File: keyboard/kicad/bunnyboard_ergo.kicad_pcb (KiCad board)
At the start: 2 copper layers, 253.5 x 103.8 mm, 58 parts, among them U2 Pico

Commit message: ergo: Pitch V2 dokumentiert, Logo mitverschoben, neu geroutet
- README: Abschnitt 'ergo variant' mit Pitch-Entscheidung (V1 Kuppenmass
  verwworfen: 0.5 mm Cap-Luecke Ring/Mittel; V2 19-mm-Raster: 4.0 mm),
  GAP-120-Begruendung und Outline-Herkunft
- vergleich_pitch.py auf GAP 120 nachgezogen (war 96)
- Kupfer-Logo G*** mitverschoben: lag nach dem Transform ausserhalb von
  Edge.Cuts (Quelle 140.69/119.17 -> Ziel frei ueber der Bank, 104/-30)
- Pipeline neu gelaufen: 260 Tracks+Vias, 0 DRC, 0 unconnected,
  0 Footprints ausserhalb des Umrisses
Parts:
- moved G*** 153.6 mm to (104.0, -30.0)

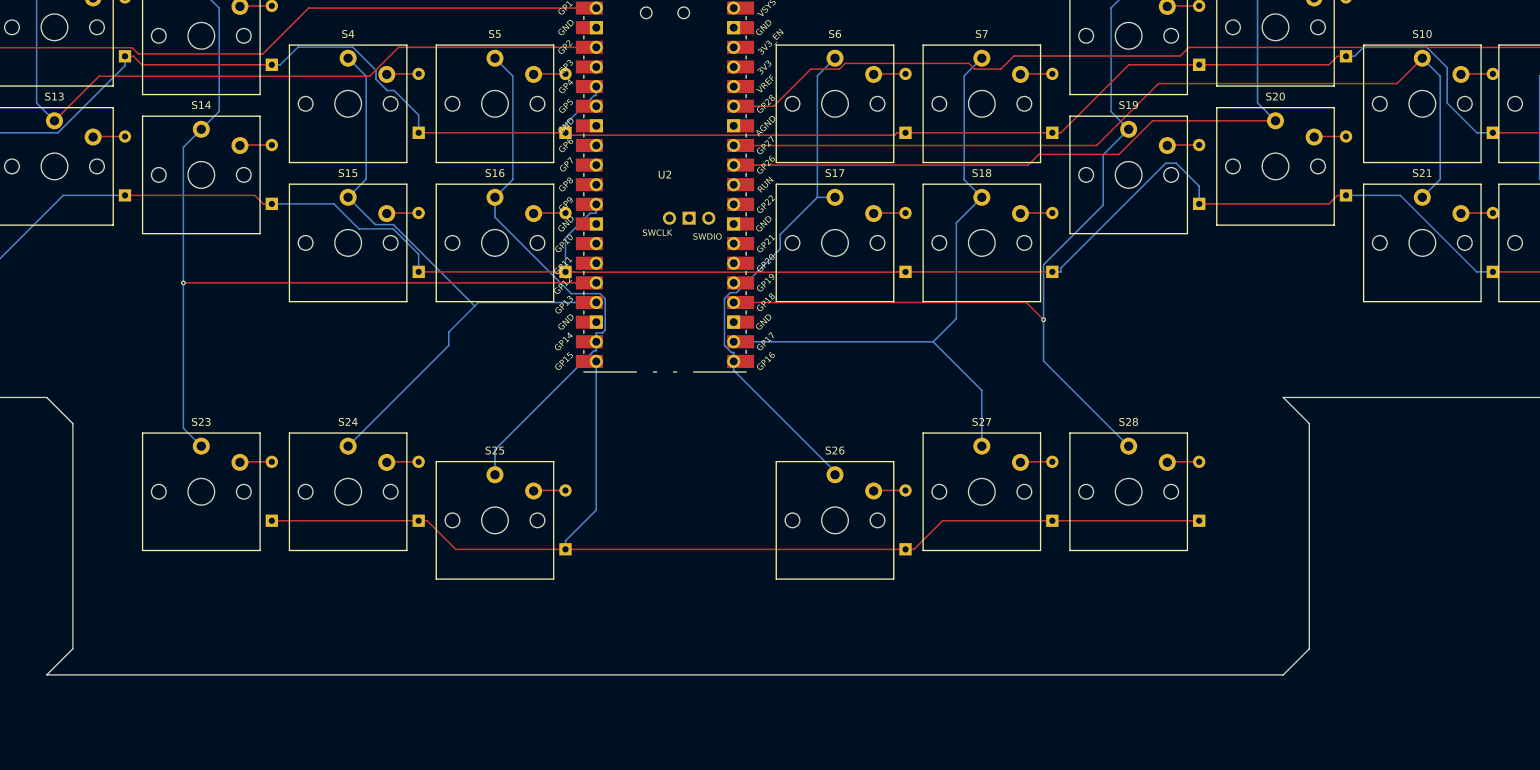
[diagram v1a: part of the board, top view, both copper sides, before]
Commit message: ergo: Daumen-Cluster korrigiert (S23/S25 vertauscht), Produktionsdaten, Viewer
Fehler gefunden beim Vergleich Quell- vs Zielboard:
- Daumen-y war S23/S28=41.0 und S25/S26=44.7 - vertauscht. STAGGER.md:
  Taste1 (A/E, Ruhepunkt) +45, Taste2 (O/U, 19 innen) +41, Extra X1/X2 +55.
  Jetzt S23/S28=44.7, S24/S27=41.0, S25/S26=55.0.
- keyboard/production/gerber.zip war das ORIGINAL vom 11.03.2024, nicht das
  Ergo-Board. Neu: keyboard/production/gerber_ergo.zip (26 Dateien) mit
  frischen Gerbern, Drill und positions.csv.

docs/ergebnis.html: selbsttragender Viewer (Bilder inline + massstaeblicher
SVG-Routingplan + Verifikationstabelle).

Verifikation: 252 Tracks, 0 DRC, 0 unconnected, min Daumen-Kappenabstand
4.36 mm, Viewer in Chromium fehlerfrei (3 Bilder dekodiert, 249 Track-Linien).
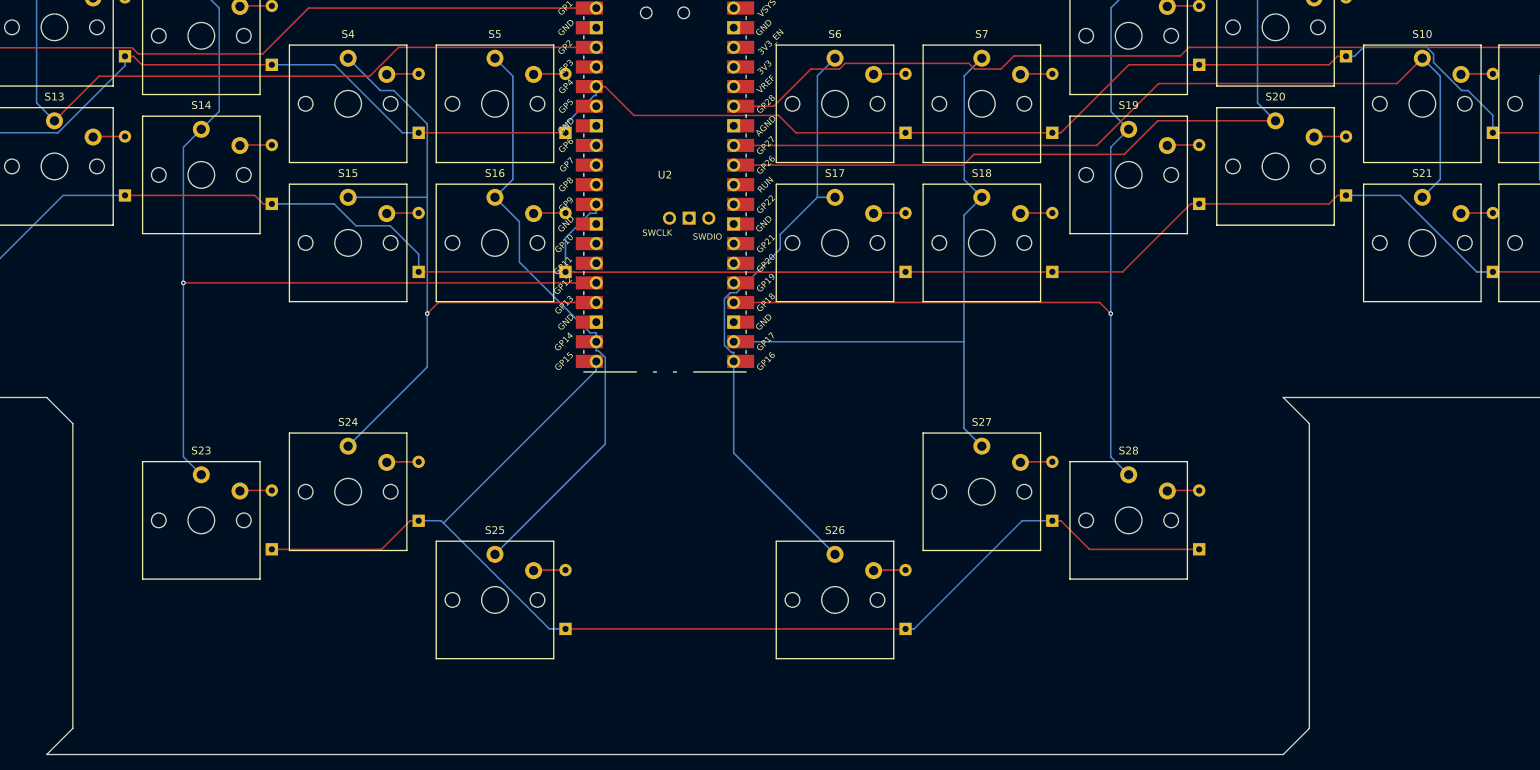
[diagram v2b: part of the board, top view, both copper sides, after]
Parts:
- moved D25 10.3 mm to (-12.9, 58.8)
- moved D26 10.3 mm to (31.1, 58.8)
- moved S25 10.3 mm to (-22.0, 55.0)
- moved S26 10.3 mm to (22.0, 55.0)
- moved D23 3.70 mm to (-50.9, 48.5)
- moved D28 3.70 mm to (69.1, 48.5)
- moved S23 3.70 mm to (-60.0, 44.7)
- moved S28 3.70 mm to (60.0, 44.7)
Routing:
- net Row 2: track 149.0 -> 163.8 mm
- net Column 5: track 68.7 -> 79.0 mm
- net Column 3: track 83.0 -> 92.4 mm, vias 0 -> 1
- net Column 4: track 70.5 -> 78.6 mm
- net Row 0: track 246.2 -> 239.8 mm
- net Row 1: track 248.1 -> 242.1 mm
- net Column 7: track 111.0 -> 115.9 mm
- net Column 2: track 116.3 -> 120.0 mm
- net Column 6: track 83.1 -> 83.8 mm
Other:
- board size 253.5 x 103.8 mm -> 253.5 x 114.1 mm

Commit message: ergo: Board kompakter - Logo raus, Rand 10.5 -> 4.0 mm
- Kupfer-Logo G*** entfernt (Dekoration, kostete Flaeche). Wichtig: Remove()
  vor dem Track-Loeschen, sonst toter SWIG-Handle (Segfault in der
  Footprint-Iteration).
- Rand vom Kappenrand zur Boardkante 10.5-12.5 -> 4.0 mm rundum. Neuer
  Umriss beruecksichtigt zusaetzlich den Pico, der 7 mm ueber die Bank ragt
  (haette sonst ausserhalb von Edge.Cuts gelegen).
- Ergebnis: 236.6 x 97.2 mm statt 253.6 x 114.2 (-17 x -17 mm).
- Kleinster Kupfer-Kante-Abstand 1.62 mm (JLCPCB-Min. 0.2 mm).
- Verifikation: 254 Tracks, 0 DRC, 0 unconnected, 0 Footprints ausserhalb,
  Rand exakt 4.0 mm auf allen vier Seiten.
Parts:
- removed G***: LOGO, Library:bunnyguy
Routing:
- net Column 7: track 115.9 -> 131.3 mm, vias 1 -> 0
- net Row 0: track 239.8 -> 242.3 mm
- net Row 1: track 242.1 -> 242.2 mm, vias 0 -> 1
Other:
- board size 253.5 x 114.1 mm -> 236.5 x 97.1 mm

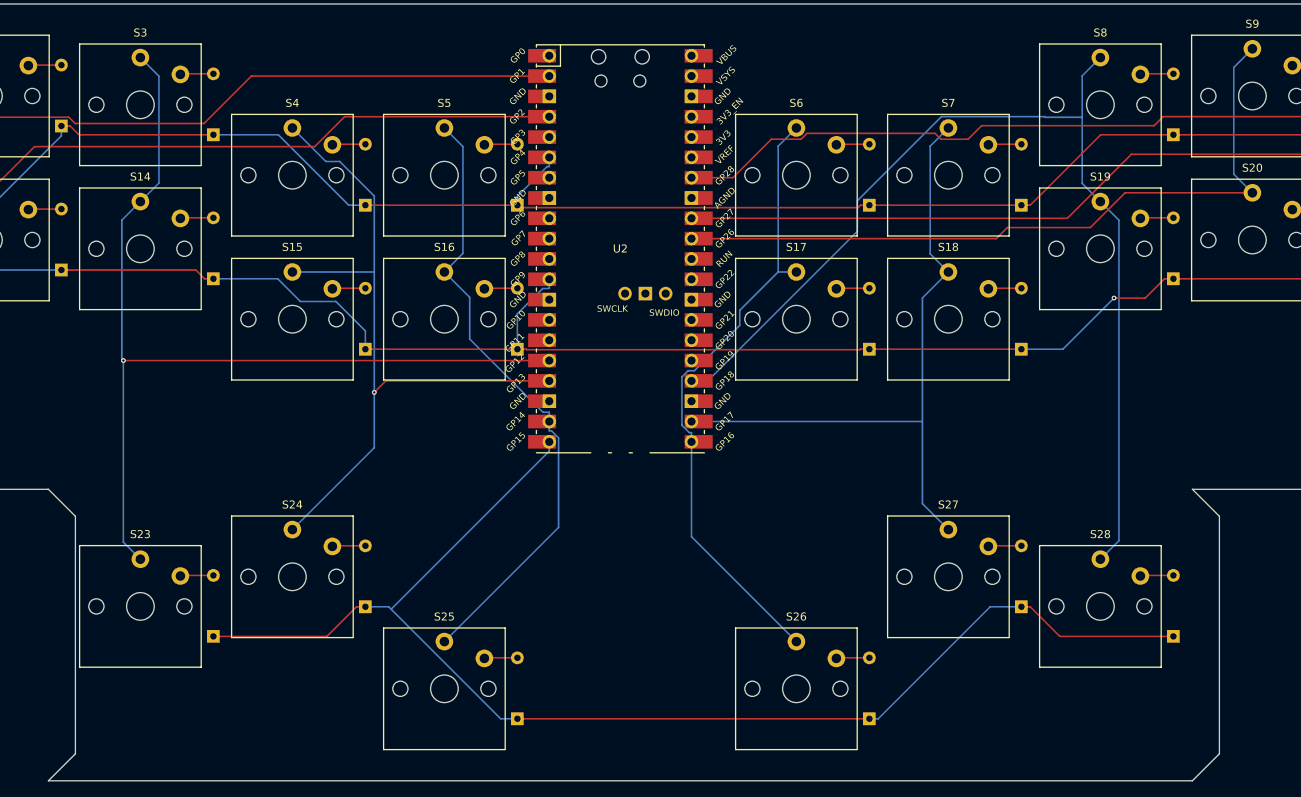
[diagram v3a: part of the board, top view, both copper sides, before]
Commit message: ergo: Daumen 3 Grad gedreht, Innen-Fase entfernt
Umriss:
- Chamfer nur noch an konvexen Ecken (4 Bank-Ecken, 2 Zungen-Enden). Der
  Bank->Zunge-Uebergang ist konkav - eine Fase schnitt dort Material weg,
  das die Ecke traegt. 16 -> 14 Punkte.

Daumen:
- Die 6 Daumentasten sind um 3 Grad zum Daumen gedreht (links negativ,
  rechts positiv). Winkel aus der Messung (Daumenachse 124-134 Grad zur
  Fingerrichtung), aber durch die Kappenbreite begrenzt.
- Choc-1u-Kappe ist 17.5 x 16.5 mm, nicht 15. Bei 12 Grad ueberlappen
  S23/S24 um 1.4 mm - Kappen stossen physisch, DRC sieht das nicht.
  3 Grad -> 0.97 mm Luecke.
- Dioden: gedrehte Tasten brauchen Offset 10.0 statt 9.125, sonst rotiert
  das eigene NPTH-Loch ins Diodenpad (1.40 statt 1.62 mm).
- D23 gespiegelt (nach aussen): mit +10.56 nur 9.96 mm von S24, kollidierte
  mit dessen Loch (0.04 mm Rand).

Verifikation: 293 Tracks, 0 DRC, 0 unconnected, 0 ausserhalb Edge.Cuts,
Kupfer-Kante 1.62 mm, Viewer in Chromium fehlerfrei.
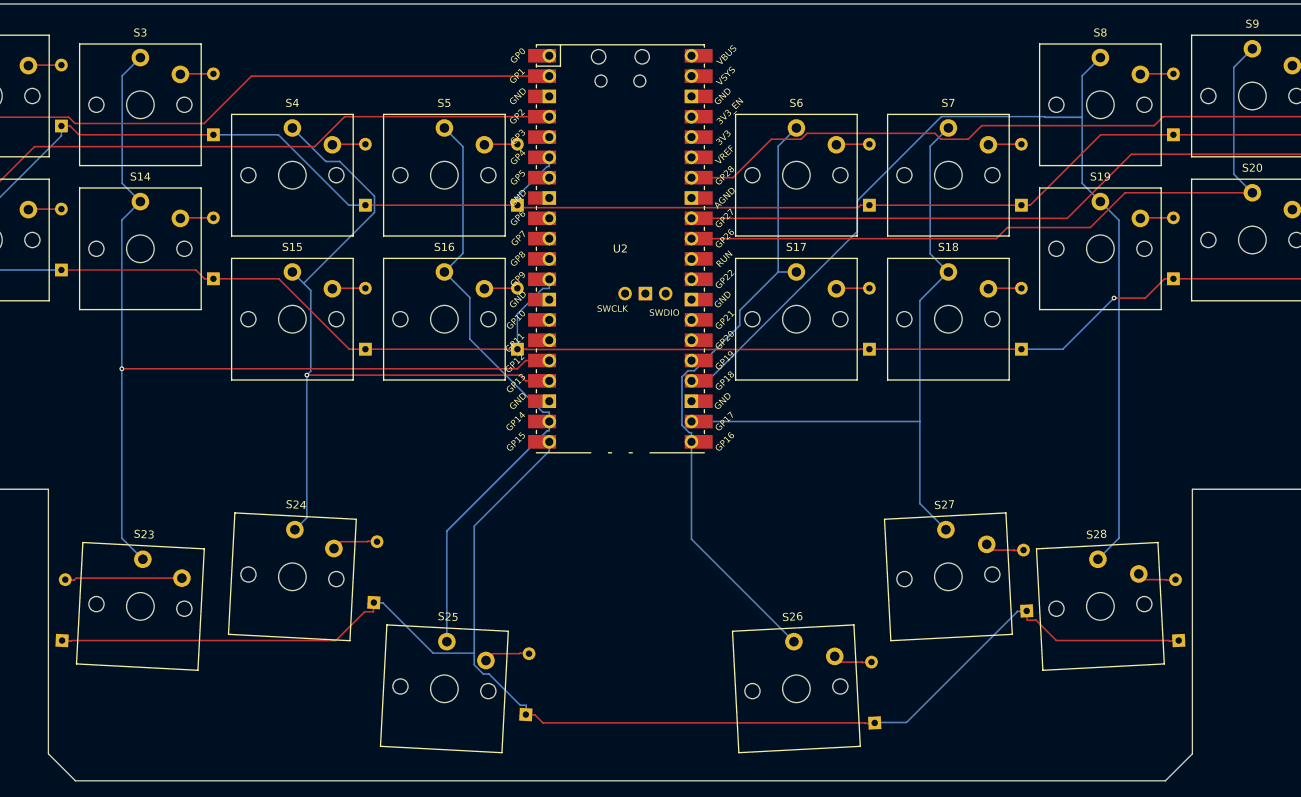
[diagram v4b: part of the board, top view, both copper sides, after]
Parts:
- moved D23 18.9 mm to (-69.8, 49.0), turned to 87 degrees
- moved D24 1.18 mm to (-30.8, 44.2), turned to 87 degrees
- moved D25 1.18 mm to (-11.8, 58.2), turned to 87 degrees
- moved D28 0.84 mm to (69.8, 49.0), turned to 93 degrees
- moved D26 0.84 mm to (31.8, 59.3), turned to 93 degrees
- moved D27 0.84 mm to (50.8, 45.3), turned to 93 degrees
- turned S23 to -3 degrees
- turned S24 to -3 degrees
- turned S25 to -3 degrees
- turned S26 to 3 degrees
- turned S27 to 3 degrees
- turned S28 to 3 degrees
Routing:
- net Row 2: track 163.8 -> 188.2 mm
- net Net-(D23-A): track 4.15 -> 14.7 mm
- net Net-(D25-A): track 4.15 -> 5.77 mm
- net Net-(D24-A): track 4.15 -> 5.77 mm
- net Row 1: track 242.2 -> 240.8 mm
- net Column 4: track 78.6 -> 77.5 mm
- net Net-(D26-A): track 4.15 -> 4.92 mm
- net Net-(D27-A): track 4.15 -> 4.92 mm
- net Net-(D28-A): track 4.15 -> 4.92 mm
- net Column 2: track 119.8 -> 120.5 mm
- net Column 3: track 92.4 -> 92.9 mm
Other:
- outline, holes or cut-outs redrawn

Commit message: ergo: Daumen rechts korrigiert (links +3, rechts -3), Dioden im Cluster entzerrt
- Drehrichtung rechts umgekehrt: vorher beide -3, jetzt links +3 / rechts -3.
  Das Choc-Footprint ist nicht spiegelsymmetrisch (alle 6 Daumentasten haben
  im Quellboard dieselbe Pad-Achse 22.78 Grad), die Spiegelung ergibt sich
  daher nicht aus dem Vorzeichen allein.
- Dioden-Offsets im Daumencluster explizit je Taste (THUMB_DIODE_OX).
  Vorher kollidierten D27 (+10 -> x=51.2) und D28 (-8 -> x=52.2) mit 1 mm
  Abstand (courtyards_overlap). Jetzt zeigen alle zur Cluster-Mitte:
  S23/S28 8.0, S24/S25/S26/S27 10.0, jeweils mit Seitenvorzeichen.
- Verifikation: 283 Tracks, 0 DRC, 0 unconnected, 0 ausserhalb Edge.Cuts,
  Board unveraendert 236.6 x 97.2 mm.
- docs/ergebnis.html: Zoom auf den rechten Daumen mit eingezeichneten
  Daumenpositionen und Kappen-Oberkanten (gelbe Markierung).
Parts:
- moved D26 19.6 mm to (12.2, 59.3), turned to 87 degrees
- moved D27 19.6 mm to (31.2, 45.3), turned to 87 degrees
- moved D23 17.6 mm to (-52.2, 48.9), turned to 93 degrees
- moved D28 17.6 mm to (52.2, 48.9), turned to 87 degrees
- moved D24 1.12 mm to (-31.2, 45.3), turned to 93 degrees
- moved D25 1.12 mm to (-12.2, 59.3), turned to 93 degrees
- turned S23 to 3 degrees
- turned S24 to 3 degrees
- turned S25 to 3 degrees
- turned S26 to -3 degrees
- turned S27 to -3 degrees
- turned S28 to -3 degrees
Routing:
- net Row 2: track 188.2 -> 148.2 mm
- net Column 7: track 131.4 -> 118.4 mm, vias 0 -> 1
- net Net-(D23-A): track 14.7 -> 2.88 mm
- net Net-(D27-A): track 4.92 -> 14.7 mm
- net Net-(D26-A): track 4.92 -> 14.7 mm
- net Column 6: track 83.5 -> 91.9 mm
- net Net-(D28-A): track 4.92 -> 12.6 mm
- net Row 1: track 240.8 -> 242.1 mm, vias 1 -> 0
- net Column 4: track 77.5 -> 78.7 mm
- net Net-(D25-A): track 5.77 -> 4.92 mm
- net Net-(D24-A): track 5.77 -> 4.92 mm

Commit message: ergo: Viewer-Bug behoben (SVG ohne Groesse), Daumen-Vorzeichen getauscht
Viewer:
- Die Plaene hatten viewBox-Werte in Pixeln, aber width/height fehlten, und
  der Zoom erbte die volle Boardhoehe (1626x2301 statt ~600x600). Deshalb war
  nichts zu sehen. Jetzt explizite width/height + eigener Crop fuer den Zoom.
- docs/ergebnis.html zeigt beide Vorzeichen-Varianten nebeneinander:
  A links +3 / rechts -3, B links -3 / rechts +3.

Daumen:
- Vorzeichen getauscht: links jetzt -3, rechts +3.
- Pipeline neu gelaufen: 290 Tracks, 0 DRC, 0 unconnected.

Umschalten ist eine Zeile in tools/ergo_transform.py (THUMB_ROT-Zeichen
in den sechs out[...]-Zeilen bei target_positions()).
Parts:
- moved D24 1.12 mm to (-30.8, 44.2), turned to 87 degrees
- moved D25 1.12 mm to (-11.8, 58.2), turned to 87 degrees
- moved D26 1.12 mm to (11.8, 58.2), turned to 93 degrees
- moved D27 1.12 mm to (30.8, 44.2), turned to 93 degrees
- moved D23 0.92 mm to (-51.8, 48.0), turned to 87 degrees
- moved D28 0.92 mm to (51.8, 48.0), turned to 93 degrees
- turned S23 to -3 degrees
- turned S24 to -3 degrees
- turned S25 to -3 degrees
- turned S26 to 3 degrees
- turned S27 to 3 degrees
- turned S28 to 3 degrees
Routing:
- net Column 7: track 118.4 -> 131.4 mm, vias 1 -> 0
- net Column 6: track 91.9 -> 83.5 mm
- net Row 2: track 148.2 -> 152.3 mm
- net Row 1: track 242.1 -> 240.8 mm, vias 0 -> 1
- net Column 4: track 78.7 -> 77.5 mm
- net Net-(D25-A): track 4.92 -> 5.77 mm
- net Net-(D26-A): track 14.7 -> 15.5 mm
- net Net-(D27-A): track 14.7 -> 15.5 mm
- net Net-(D24-A): track 4.92 -> 5.77 mm
- net Net-(D28-A): track 12.6 -> 13.5 mm
- net Net-(D23-A): track 2.88 -> 3.73 mm

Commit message: ergo: Daumen-Vorzeichen auf die am PCB bestaetigte Variante A zurueck
- Vorzeichen wieder links +3 / rechts -3. Der Tausch auf B in 2685737 war
  falsch (Nutzer hat A am PCB bestaetigt).
- Nur S23-S28 werden gedreht; S1-S22 und der Pico bleiben bei rot = 0.
- Veralteten Kommentar korrigiert: der Winkel kommt nicht aus der gemessenen
  Daumenachse (125-134 Grad), sondern ist durch die Kappenbreite begrenzt.
- Viewer: beide Daumen-Cluster einzeln im Zoom statt einer Vorzeichen-
  Gegenueberstellung, da die Richtung jetzt feststeht.
- 283 Tracks, 0 DRC, 0 unconnected.
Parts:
- moved D24 1.12 mm to (-31.2, 45.3), turned to 93 degrees
- moved D25 1.12 mm to (-12.2, 59.3), turned to 93 degrees
- moved D26 1.12 mm to (12.2, 59.3), turned to 87 degrees
- moved D27 1.12 mm to (31.2, 45.3), turned to 87 degrees
- moved D23 0.92 mm to (-52.2, 48.9), turned to 93 degrees
- moved D28 0.92 mm to (52.2, 48.9), turned to 87 degrees
- turned S23 to 3 degrees
- turned S24 to 3 degrees
- turned S25 to 3 degrees
- turned S26 to -3 degrees
- turned S27 to -3 degrees
- turned S28 to -3 degrees
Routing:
- net Column 7: track 131.4 -> 118.4 mm, vias 0 -> 1
- net Column 6: track 83.5 -> 91.9 mm
- net Row 2: track 152.3 -> 148.2 mm
- net Row 1: track 240.8 -> 242.1 mm, vias 1 -> 0
- net Column 4: track 77.5 -> 78.7 mm
- net Net-(D26-A): track 15.5 -> 14.7 mm
- net Net-(D25-A): track 5.77 -> 4.92 mm
- net Net-(D27-A): track 15.5 -> 14.7 mm
- net Net-(D24-A): track 5.77 -> 4.92 mm
- net Net-(D28-A): track 13.5 -> 12.6 mm
- net Net-(D23-A): track 3.73 -> 2.88 mm

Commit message: ergo: Daumen links/rechts entgegengesetzt gedreht, Plan in Render-Orientierung
- Links -3 Grad, rechts +3 Grad. Vorher drehten beide Seiten gleichsinnig
  (Render-Achse beide -19.78 bzw. beide -25.78), die Kappen kippten also
  nicht gespiegelt zueinander.
- Nachweis ueber die Pad-Achse im Render-Koordinatensystem (y nach oben):
  links -25.78 Grad, rechts -19.78 Grad -> gespiegelt.
- Plan (docs/ergebnis.html) wird jetzt in derselben Orientierung wie der
  3D-Render gezeichnet (y gespiegelt, Rotationswinkel negiert). Vorher
  zeigte der Plan y nach unten und damit alle Drehungen optisch entgegen-
  gesetzt zum Render - das war der Grund, warum Plan und PCB nie
  gleichzeitig stimmten.
- 290 Tracks, 0 DRC, 0 unconnected.
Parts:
- moved D24 1.12 mm to (-30.8, 44.2), turned to 87 degrees
- moved D25 1.12 mm to (-11.8, 58.2), turned to 87 degrees
- moved D26 1.12 mm to (11.8, 58.2), turned to 93 degrees
- moved D27 1.12 mm to (30.8, 44.2), turned to 93 degrees
- moved D23 0.92 mm to (-51.8, 48.0), turned to 87 degrees
- moved D28 0.92 mm to (51.8, 48.0), turned to 93 degrees
- turned S23 to -3 degrees
- turned S24 to -3 degrees
- turned S25 to -3 degrees
- turned S26 to 3 degrees
- turned S27 to 3 degrees
- turned S28 to 3 degrees
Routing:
- net Column 7: track 118.4 -> 131.4 mm, vias 1 -> 0
- net Column 6: track 91.9 -> 83.5 mm
- net Row 2: track 148.2 -> 152.3 mm
- net Row 1: track 242.1 -> 240.8 mm, vias 0 -> 1
- net Column 4: track 78.7 -> 77.5 mm
- net Net-(D26-A): track 14.7 -> 15.5 mm
- net Net-(D25-A): track 4.92 -> 5.77 mm
- net Net-(D27-A): track 14.7 -> 15.5 mm
- net Net-(D24-A): track 4.92 -> 5.77 mm
- net Net-(D28-A): track 12.6 -> 13.5 mm
- net Net-(D23-A): track 2.88 -> 3.73 mm
